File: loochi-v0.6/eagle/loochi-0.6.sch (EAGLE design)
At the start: 51 parts, among them IC1 ATTINY61M, J2 POWER_JACKSMT3, Q1 PMN25ENSOT457, Q2 PMN25ENSOT457, Q3 PMN25ENSOT457, U1 BLE112, U2 LZ4-00MC00BIGPADS, U3 LP2985

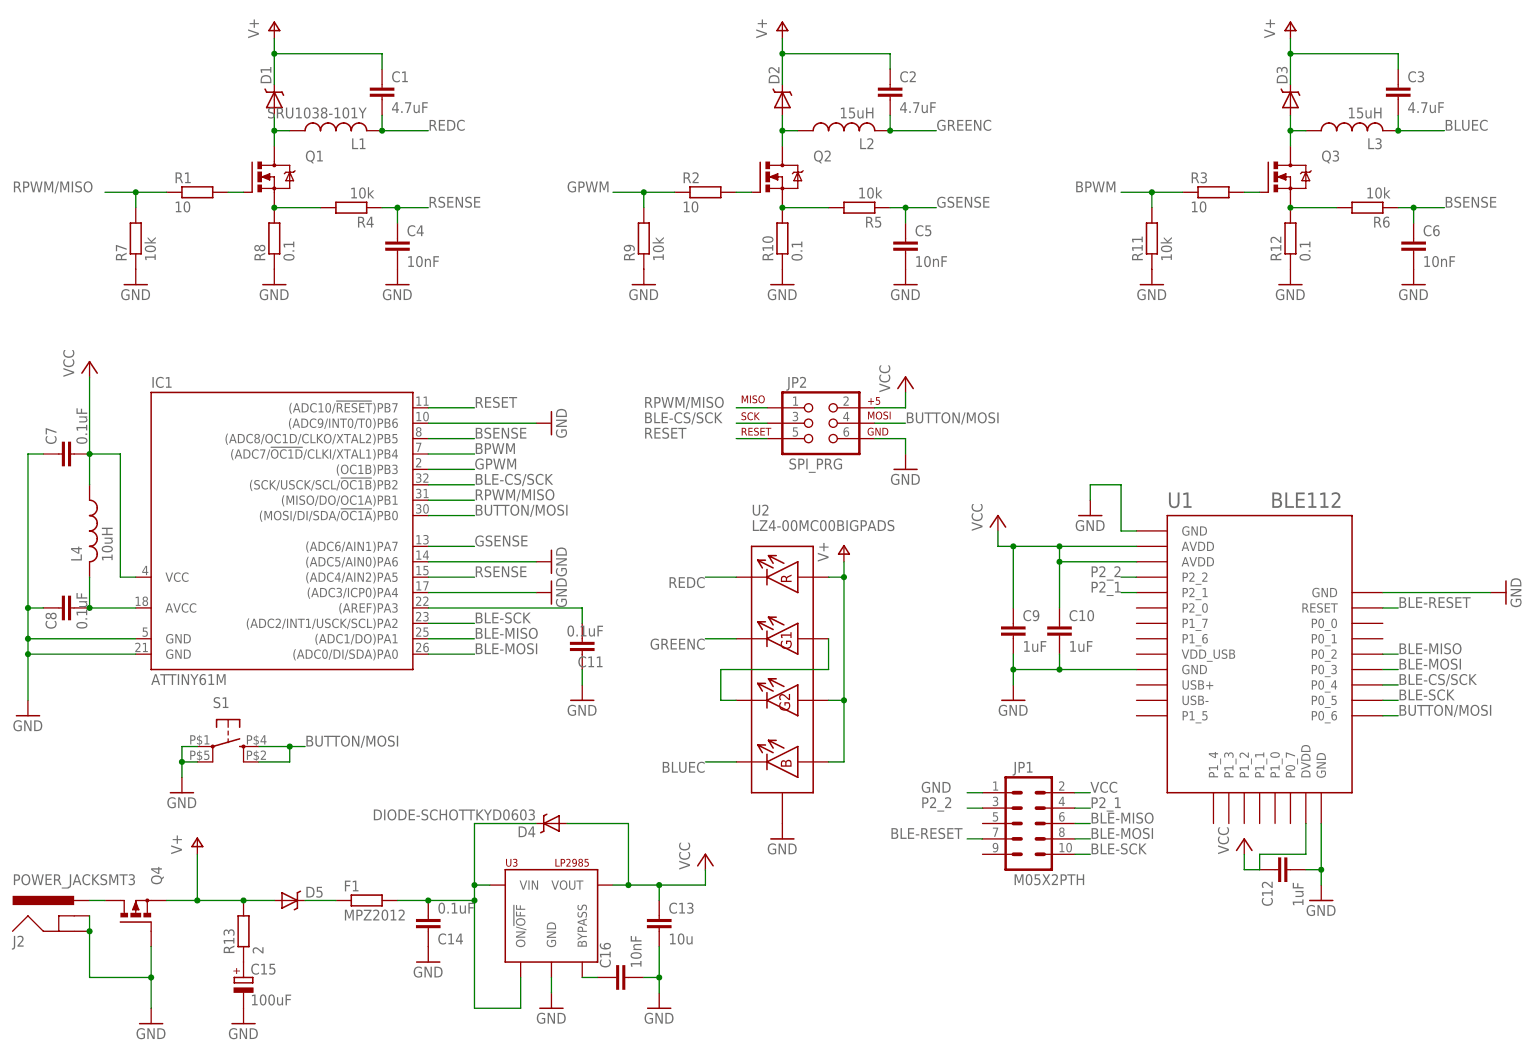
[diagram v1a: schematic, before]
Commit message: Final changes before ordering the board (minor cosmetic changes)
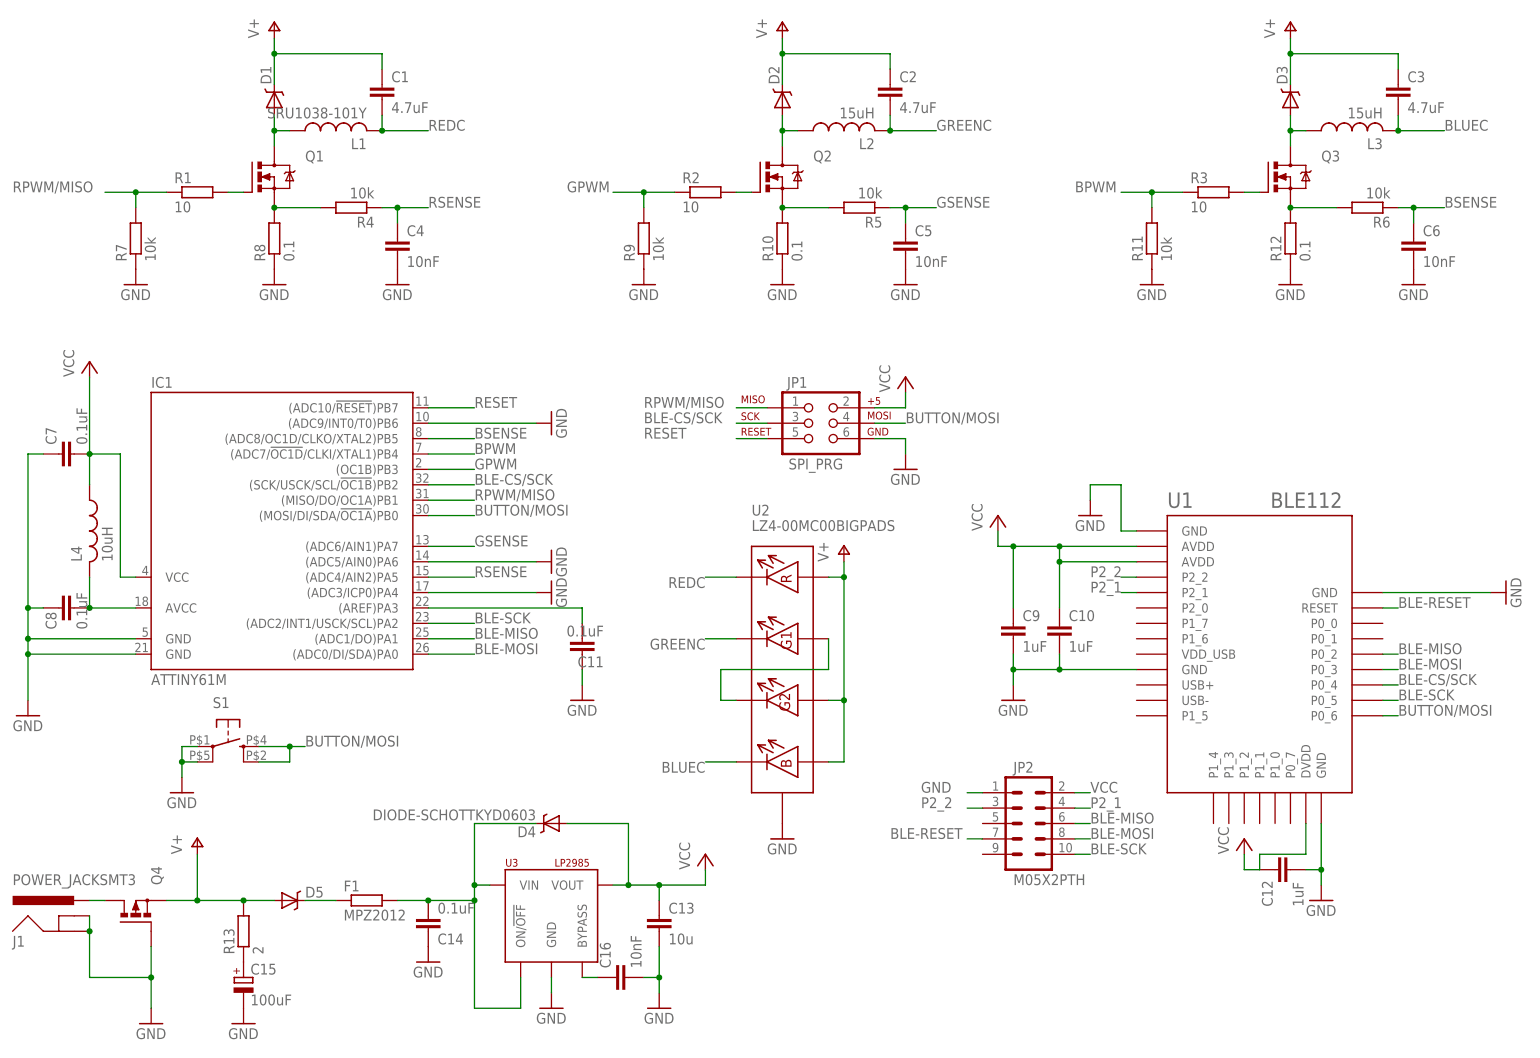
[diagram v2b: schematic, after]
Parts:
- JP1: value M05X2PTH -> SPI_PRG; device SparkFun:M05X2PTH -> SparkFun:AVR_SPI_PRG_6NS
- JP2: value SPI_PRG -> M05X2PTH; device SparkFun:AVR_SPI_PRG_6NS -> SparkFun:M05X2PTH
- renumbered J2 to J1
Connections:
- net BLE-CS/SCK: now also JP1.3; no longer JP2.3
- net BLE-MISO: now also JP2.6; no longer JP1.6
- net BLE-MOSI: now also JP2.8; no longer JP1.8
- net BLE-RESET: now also JP2.7; no longer JP1.7
- net BLE-SCK: now also JP2.10; no longer JP1.10
- net BUTTON/MOSI: now also JP1.4; no longer JP2.4
- net GND: now also JP1.6, JP2.1; no longer JP1.1, JP2.6
- net P2_1: now also JP2.4; no longer JP1.4
- net P2_2: now also JP2.3; no longer JP1.3
- net RESET: now also JP1.5; no longer JP2.5
- net RPWM/MISO: now also JP1.1; no longer JP2.1
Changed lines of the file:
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@@
 </classes>
 <parts>
-<part name="J2" library="power-connectors" deviceset="POWER_JACK" device="SMT3"/>
-<part name="JP2" library="SparkFun" deviceset="AVR_SPI_PRG_6" device="NS" value="SPI_PRG"/>
+<part name="J1" library="power-connectors" deviceset="POWER_JACK" device="SMT3"/>
+<part name="JP1" library="SparkFun" deviceset="AVR_SPI_PRG_6" device="NS" value="SPI_PRG"/>
 <part name="C7" library="rcl" deviceset="C-EU" device="C0603" value="0.1uF"/>
 <part name="C8" library="rcl" deviceset="C-EU" device="C0603" value="0.1uF"/>
@@
 <part name="D5" library="diode-schottky" deviceset="DIODE-SCHOTTKY" device="" value="PMEG4010CEH"/>
 <part name="S1" library="buttons" deviceset="TAC_SWITCH" device=""/>
-<part name="JP1" library="SparkFun" deviceset="M05X2" device="PTH"/>
+<part name="JP2" library="SparkFun" deviceset="M05X2" device="PTH"/>
 </parts>
 <sheets>
@@
 </plain>
 <instances>
-<instance part="J2" gate="G$1" x="15.24" y="20.32"/>
-<instance part="JP2" gate="G$1" x="137.16" y="106.68"/>
+<instance part="J1" gate="G$1" x="15.24" y="20.32"/>
+<instance part="JP1" gate="G$1" x="137.16" y="106.68"/>
 <instance part="C7" gate="G$1" x="12.7" y="101.6" smashed="yes" rot="R90">
 <attribute name="NAME" x="12.319" y="103.124" size="1.778" layer="95" rot="R90"/>
@@
 </instance>
 <instance part="S1" gate="S" x="40.64" y="53.34"/>
-<instance part="JP1" gate="G$1" x="172.72" y="40.64"/>
+<instance part="JP2" gate="G$1" x="172.72" y="40.64"/>
 </instances>
 <busses>
@@
 <net name="BUTTON/MOSI" class="0">
 <segment>
-<pinref part="JP2" gate="G$1" pin="4"/>
+<pinref part="JP1" gate="G$1" pin="4"/>
 <wire x1="147.32" y1="106.68" x2="152.4" y2="106.68" width="0.1524" layer="91"/>
 <label x="152.4" y="106.68" size="1.778" layer="95"/>
@@
 <net name="RESET" class="0">
 <segment>
-<pinref part="JP2" gate="G$1" pin="5"/>
+<pinref part="JP1" gate="G$1" pin="5"/>
 <wire x1="129.54" y1="104.14" x2="124.46" y2="104.14" width="0.1524" layer="91"/>
 <label x="109.22" y="104.14" size="1.778" layer="95"/>
@@
 <net name="BLE-CS/SCK" class="0">
 <segment>
-<pinref part="JP2" gate="G$1" pin="3"/>
+<pinref part="JP1" gate="G$1" pin="3"/>
 <wire x1="129.54" y1="106.68" x2="124.46" y2="106.68" width="0.1524" layer="91"/>
 <label x="109.22" y="106.68" size="1.778" layer="95"/>
@@
 </segment>
 <segment>
-<pinref part="JP2" gate="G$1" pin="6"/>
+<pinref part="JP1" gate="G$1" pin="6"/>
 <wire x1="147.32" y1="104.14" x2="152.4" y2="104.14" width="0.1524" layer="91"/>
 <wire x1="152.4" y1="104.14" x2="152.4" y2="101.6" width="0.1524" layer="91"/>
@@
 <pinref part="GND4" gate="1" pin="GND"/>
 <wire x1="27.94" y1="15.24" x2="27.94" y2="10.16" width="0.1524" layer="91"/>
-<pinref part="J2" gate="G$1" pin="GNDBREAK"/>
-<pinref part="J2" gate="G$1" pin="GND"/>
+<pinref part="J1" gate="G$1" pin="GNDBREAK"/>
+<pinref part="J1" gate="G$1" pin="GND"/>
 <wire x1="17.78" y1="25.4" x2="17.78" y2="22.86" width="0.1524" layer="91"/>
 <wire x1="17.78" y1="22.86" x2="17.78" y2="15.24" width="0.1524" layer="91"/>
@@
 </segment>
 <segment>
-<pinref part="JP1" gate="G$1" pin="1"/>
+<pinref part="JP2" gate="G$1" pin="1"/>
 <wire x1="165.1" y1="45.72" x2="162.56" y2="45.72" width="0.1524" layer="91"/>
 <label x="154.94" y="45.72" size="1.778" layer="95"/>
@@
 </segment>
 <segment>
-<pinref part="JP2" gate="G$1" pin="2"/>
+<pinref part="JP1" gate="G$1" pin="2"/>
 <wire x1="147.32" y1="109.22" x2="152.4" y2="109.22" width="0.1524" layer="91"/>
 <wire x1="152.4" y1="109.22" x2="152.4" y2="111.76" width="0.1524" layer="91"/>
@@
 </segment>
 <segment>
-<pinref part="JP1" gate="G$1" pin="2"/>
+<pinref part="JP2" gate="G$1" pin="2"/>
 <wire x1="180.34" y1="45.72" x2="182.88" y2="45.72" width="0.1524" layer="91"/>
 <label x="182.88" y="45.72" size="1.778" layer="95"/>
@@
 <net name="N$10" class="0">
 <segment>
-<pinref part="J2" gate="G$1" pin="PWR"/>
+<pinref part="J1" gate="G$1" pin="PWR"/>
 <pinref part="Q4" gate="G$1" pin="D"/>
 <wire x1="17.78" y1="27.94" x2="20.32" y2="27.94" width="0.1524" layer="91"/>
@@
 </segment>
 <segment>
-<pinref part="JP1" gate="G$1" pin="8"/>
+<pinref part="JP2" gate="G$1" pin="8"/>
 <wire x1="180.34" y1="38.1" x2="182.88" y2="38.1" width="0.1524" layer="91"/>
 <label x="182.88" y="38.1" size="1.778" layer="95"/>
@@
 </segment>
 <segment>
-<pinref part="JP1" gate="G$1" pin="10"/>
+<pinref part="JP2" gate="G$1" pin="10"/>
 <wire x1="180.34" y1="35.56" x2="182.88" y2="35.56" width="0.1524" layer="91"/>
 <label x="182.88" y="35.56" size="1.778" layer="95"/>
@@
 </segment>
 <segment>
-<pinref part="JP1" gate="G$1" pin="6"/>
+<pinref part="JP2" gate="G$1" pin="6"/>
 <wire x1="180.34" y1="40.64" x2="182.88" y2="40.64" width="0.1524" layer="91"/>
 <label x="182.88" y="40.64" size="1.778" layer="95"/>
@@
 </segment>
 <segment>
-<pinref part="JP2" gate="G$1" pin="1"/>
+<pinref part="JP1" gate="G$1" pin="1"/>
 <wire x1="129.54" y1="109.22" x2="124.46" y2="109.22" width="0.1524" layer="91"/>
 <label x="109.22" y="109.22" size="1.778" layer="95"/>
@@
 </segment>
 <segment>
-<pinref part="JP1" gate="G$1" pin="3"/>
+<pinref part="JP2" gate="G$1" pin="3"/>
 <wire x1="165.1" y1="43.18" x2="162.56" y2="43.18" width="0.1524" layer="91"/>
 <label x="154.94" y="43.18" size="1.778" layer="95"/>
@@
 </segment>
 <segment>
-<pinref part="JP1" gate="G$1" pin="4"/>
+<pinref part="JP2" gate="G$1" pin="4"/>
 <wire x1="180.34" y1="43.18" x2="182.88" y2="43.18" width="0.1524" layer="91"/>
 <label x="182.88" y="43.18" size="1.778" layer="95"/>
@@
 </segment>
 <segment>
-<pinref part="JP1" gate="G$1" pin="7"/>
+<pinref part="JP2" gate="G$1" pin="7"/>
 <wire x1="165.1" y1="38.1" x2="162.56" y2="38.1" width="0.1524" layer="91"/>
 <label x="149.86" y="38.1" size="1.778" layer="95"/>

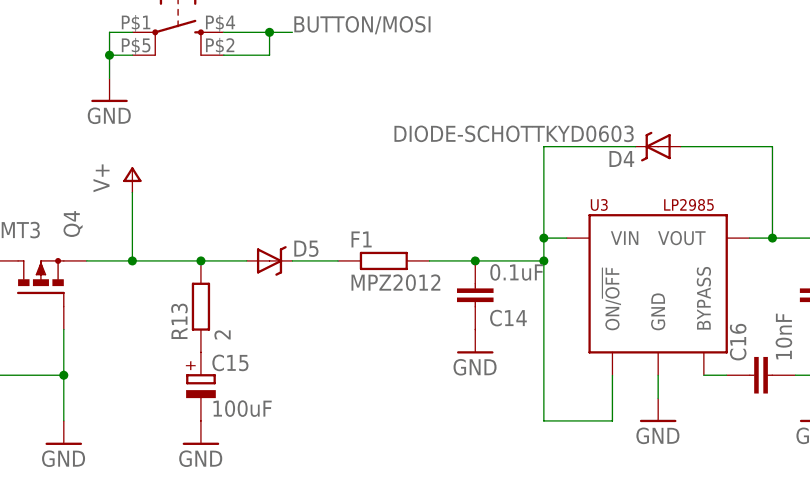
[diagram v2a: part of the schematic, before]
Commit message: Fixing reference of F1 (we want a 0603)
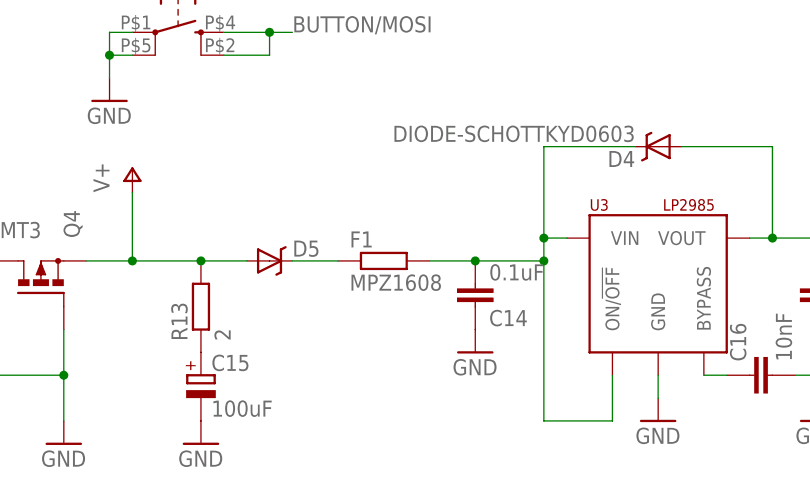
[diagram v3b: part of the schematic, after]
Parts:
- F1: value MPZ2012 -> MPZ1608
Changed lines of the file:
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@@
 <part name="GND18" library="supply1" deviceset="GND" device=""/>
 <part name="R13" library="rcl" deviceset="R-EU_" device="R0603" value="2"/>
-<part name="F1" library="rcl" deviceset="R-EU_" device="R0603" value="MPZ2012"/>
+<part name="F1" library="rcl" deviceset="R-EU_" device="R0603" value="MPZ1608"/>
 <part name="C14" library="rcl" deviceset="C-EU" device="C0603K" value="0.1uF"/>
 <part name="GND28" library="supply1" deviceset="GND" device=""/>
